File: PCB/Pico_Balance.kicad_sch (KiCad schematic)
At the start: 25 parts, among them Q1 NMOS, U1 BMI160, U2 DRV8876PWPR, U4 LM74610QDGKRQ1, U5 LMR51430

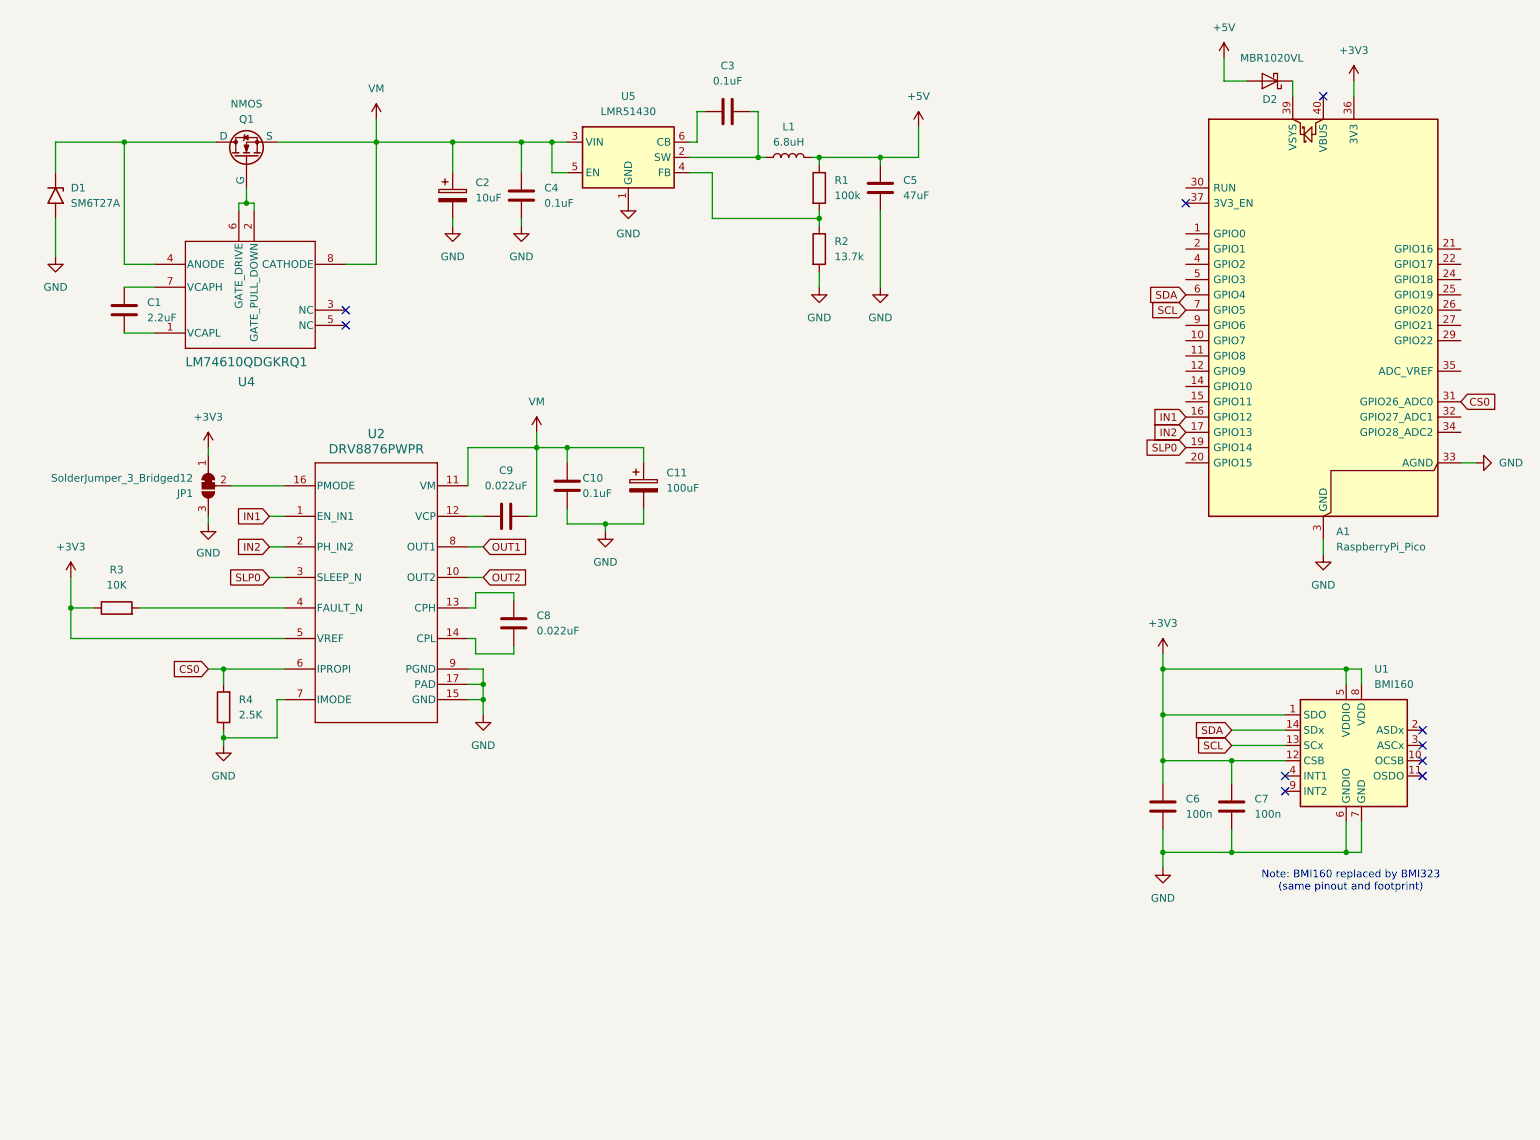
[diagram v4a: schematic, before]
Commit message: Second Motor Driver on Schematic
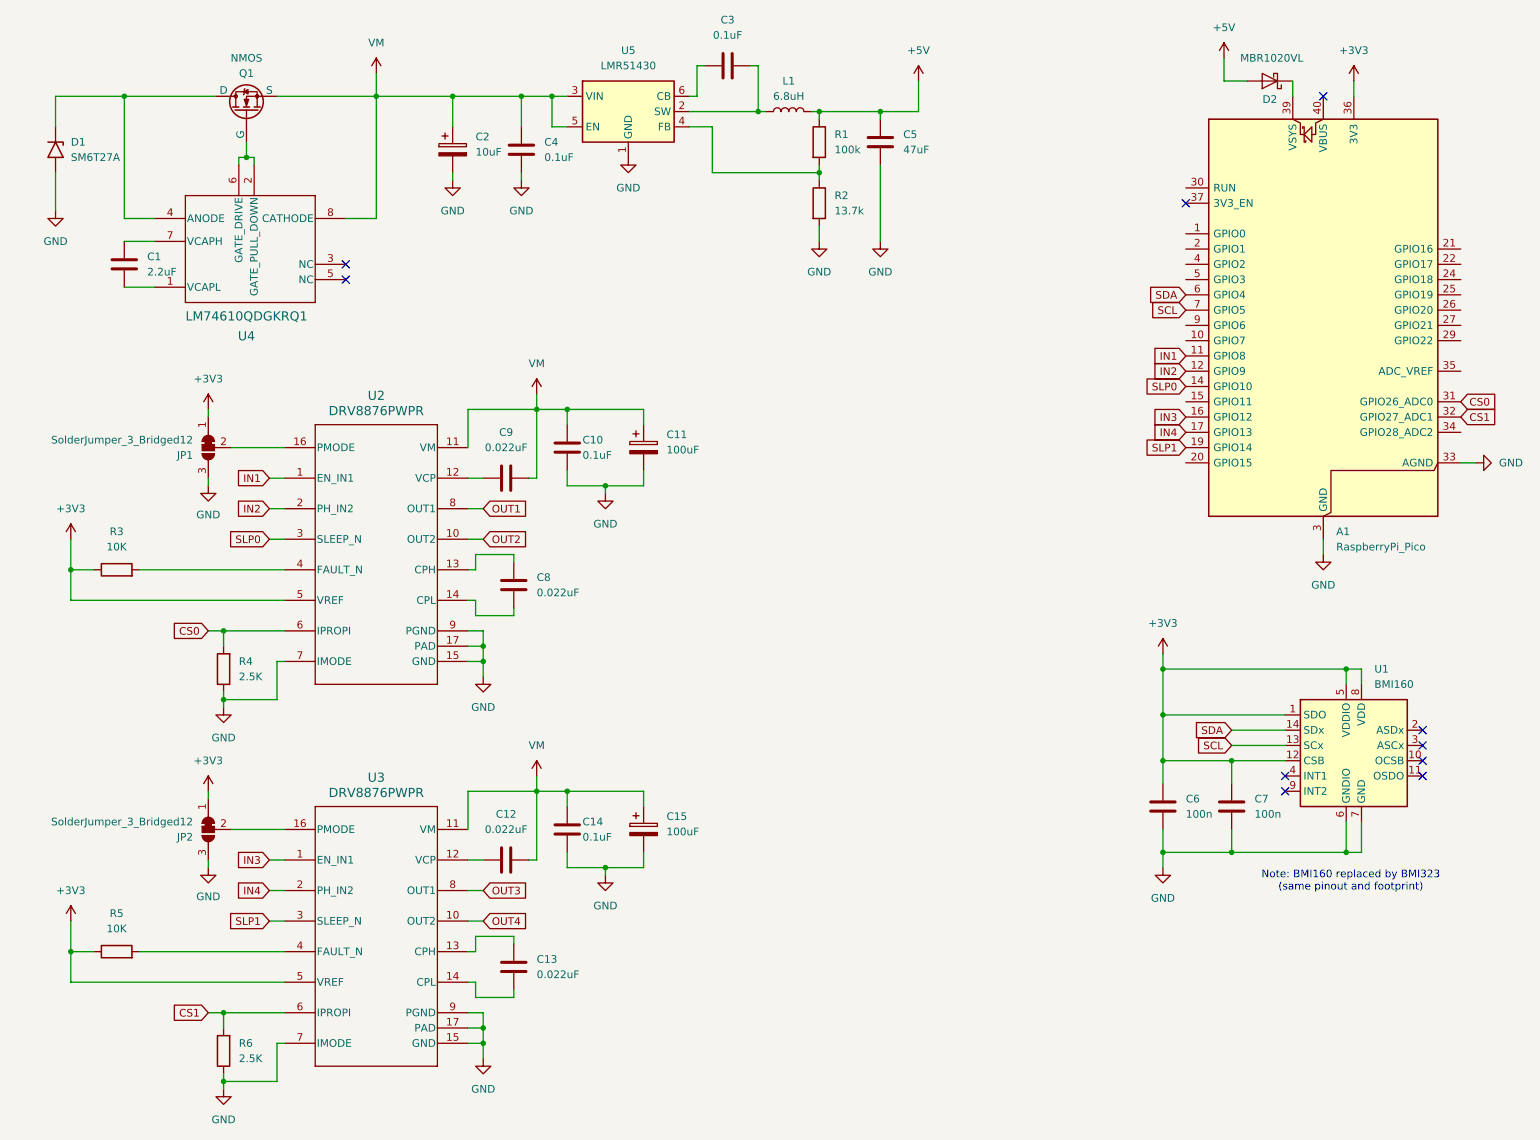
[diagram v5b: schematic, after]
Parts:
- added C12, C13: 0.022uF, symbol Device:C
- added C14: 0.1uF, symbol Device:C
- added C15: 100uF, symbol Device:C_Polarized
- added JP2: SolderJumper_3_Bridged12, Jumper:SolderJumper-3_P1.3mm_Bridged12_Pad1.0x1.5mm_NumberLabels, symbol Jumper:SolderJumper_3_Bridged12
- added R5: 10K, symbol Device:R
- added R6: 2.5K, symbol Device:R
- added U3: DRV8876PWPR, PWP0016J_N, symbol 2025-06-21_13-03-58:DRV8876PWPR
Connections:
- net +3V3: now also JP2.1 (A), R5.1, U3.5 (VREF)
- net GND: now also C14.2, C15.2, JP2.3 (B), R6.1, U3.15 (GND), U3.17 (PAD), U3.7 (IMODE), U3.9 (PGND)
- net IN1: now also A1.11 (GPIO8); no longer A1.16 (GPIO12)
- net IN2: now also A1.12 (GPIO9); no longer A1.17 (GPIO13)
- net SLP0: now also A1.14 (GPIO10); no longer A1.19 (GPIO14)
- net VM: now also C12.2, C14.1, C15.1, U3.11 (VM)
- net CS1: now reaches A1.32 (GPIO27_ADC1)
- net CS1: now also R6.2, U3.6 (IPROPI)
- new net: JP2.2 (C), U3.16 (PMODE)
- new net: C12.1, U3.12 (VCP)
- new net: C13.1, U3.13 (CPH)
- new net: C13.2, U3.14 (CPL)
- new net: R5.2, U3.4 (FAULT_N)
- new net IN3: A1.16 (GPIO12), U3.1 (EN_IN1)
- new net IN4: A1.17 (GPIO13), U3.2 (PH_IN2)
- new net OUT3: U3.8 (OUT1)
- new net OUT4: U3.10 (OUT2)
- new net SLP1: A1.19 (GPIO14), U3.3 (SLEEP_N)
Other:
- moved on the sheet: C1, C10, C11, C2, C3, C4, C5, C8, C9, D1, JP1, L1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
